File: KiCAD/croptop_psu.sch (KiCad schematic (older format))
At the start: 40 parts, among them J3 5V USB, U2 REG71055, U3 FAN5333BSX, U4 MIC23050, U5 TC1014

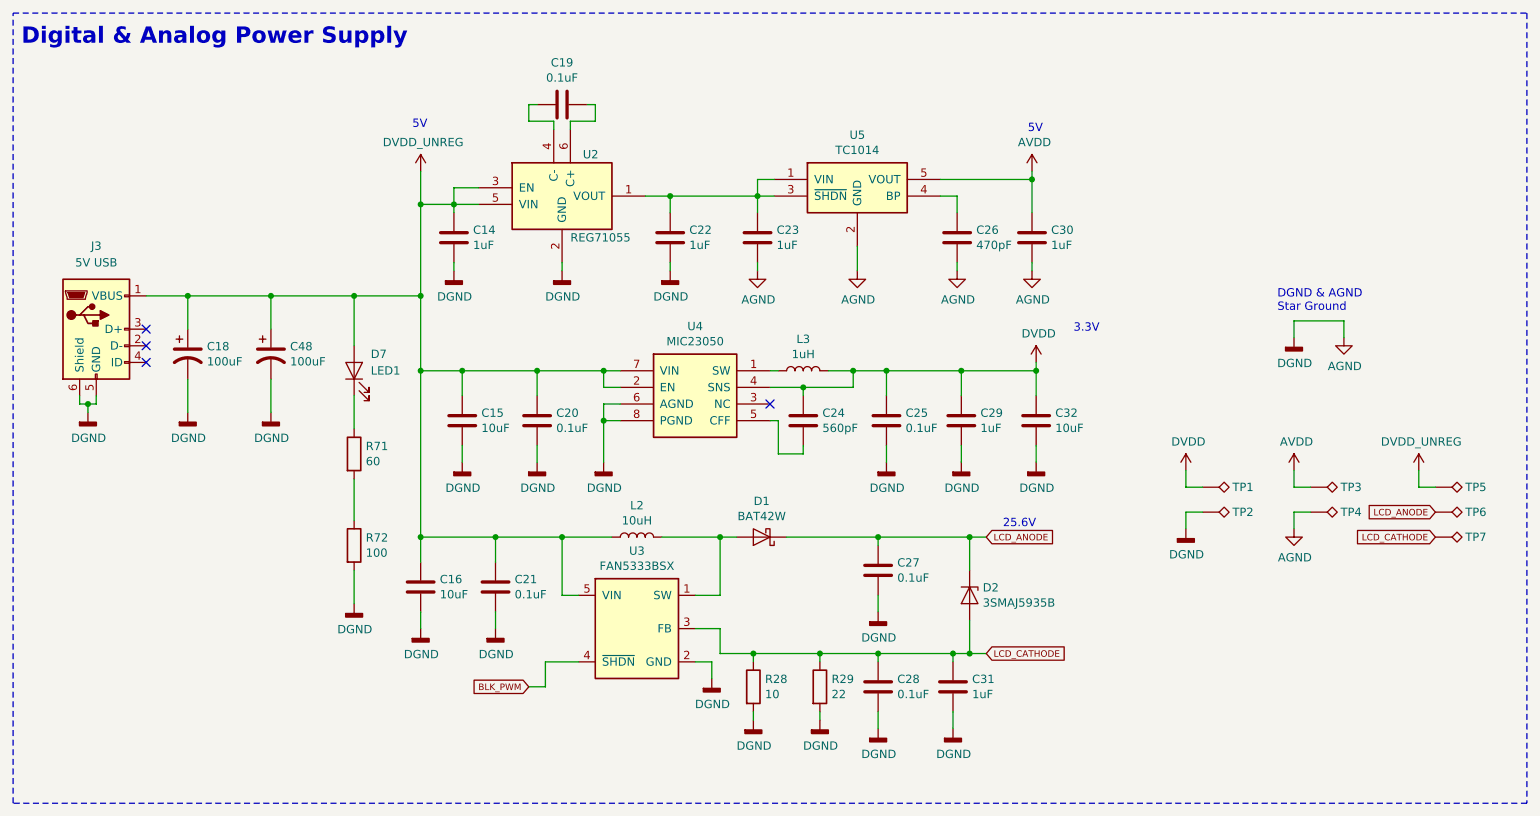
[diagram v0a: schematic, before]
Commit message: Got to PCB layout
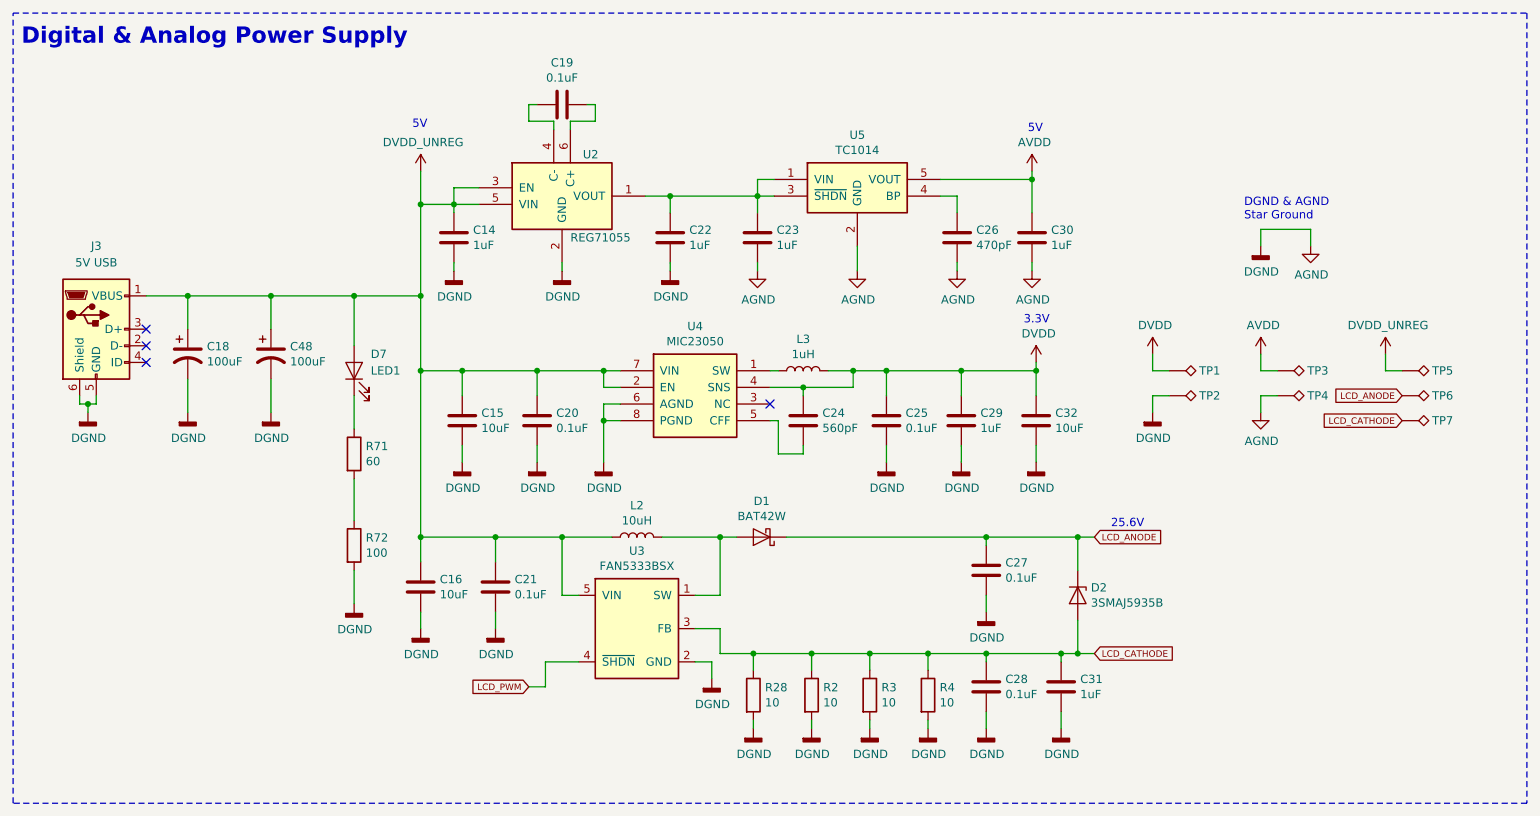
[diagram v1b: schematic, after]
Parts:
- removed R29: 22, Resistor_SMD:R_0402_1005Metric, symbol Device:R
- added R2, R3, R4: 10, Resistor_SMD:R_0402_1005Metric, symbol Device:R
- D1: footprint (none) -> croptop:D_SOD-123
- D2: footprint (none) -> croptop:DO-214AC
- J3: footprint (none) -> croptop:USB_Micro-B_Molex_47346-0001
- L2: footprint (none) -> Inductor_SMD:L_1210_3225Metric
- L3: footprint (none) -> Inductor_SMD:L_0805_2012Metric
- U4: footprint Package_DFN_QFN:Micrel_MLF-8-1EP_2x2mm_P0.5mm_EP0.8x1.3mm_ThermalVias -> Package_DFN_QFN:DFN-8-1EP_2x2mm_P0.45mm_EP0.64x1.38mm
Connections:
- net AGND: now also R2.2, R3.2, R4.2
- net LCD_CATHODE: now also R2.1, R3.1, R4.1
- net BLK_PWM renamed LCD_PWM
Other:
- moved on the sheet: C27, C28, C31, D2, R28, TP1, TP2, TP3, TP4, TP5, TP6, TP7

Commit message: Final board shape
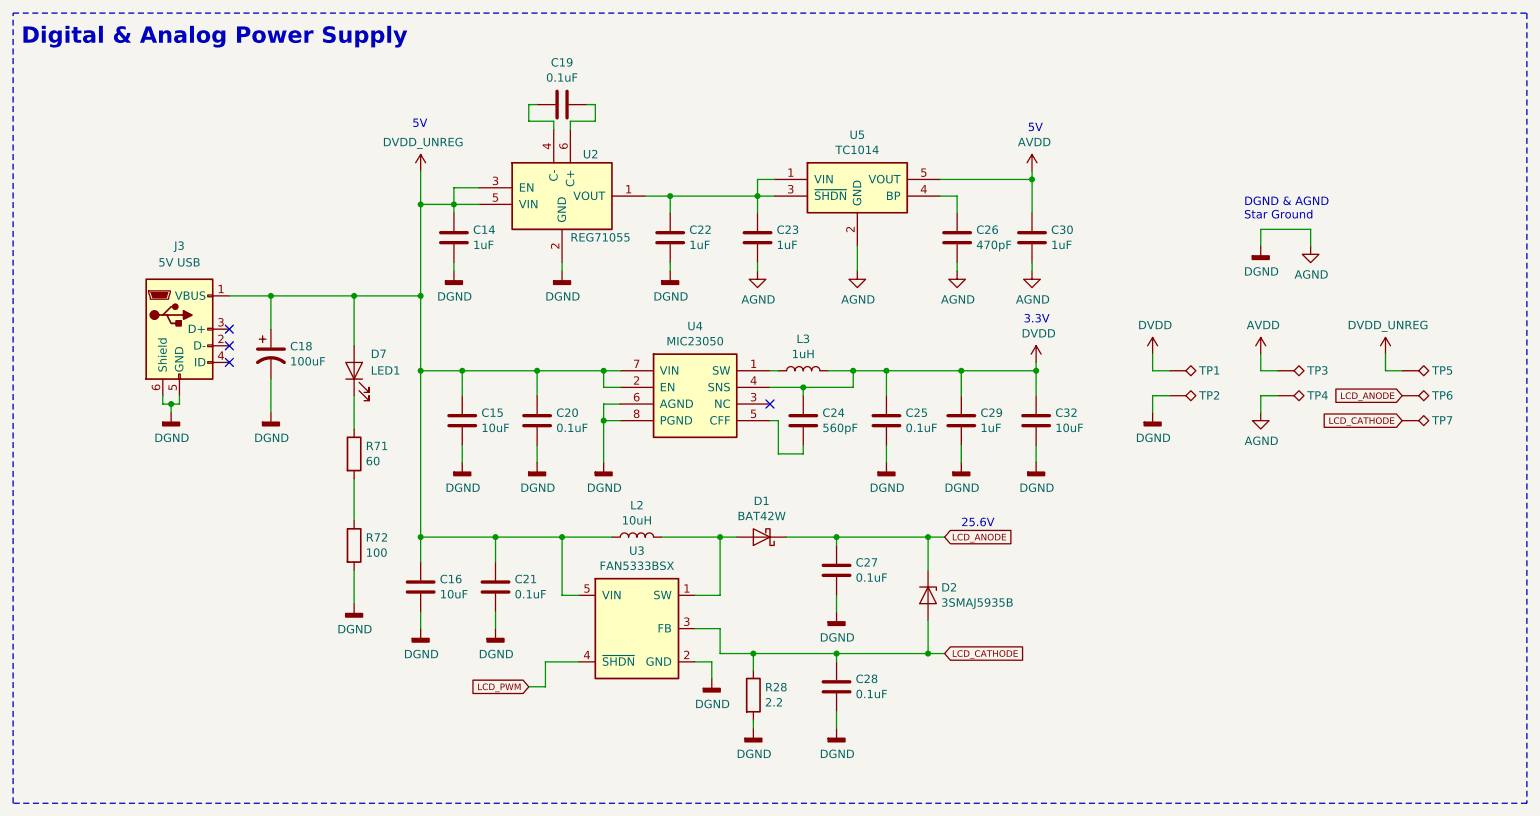
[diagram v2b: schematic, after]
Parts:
- removed C31: 1uF, Capacitor_SMD:C_0402_1005Metric, symbol Device:C
- removed C48: 100uF, Capacitor_SMD:CP_Elec_6.3x7.7, symbol Device:CP1
- removed R2, R3, R4: 10, Resistor_SMD:R_0402_1005Metric, symbol Device:R
- R28: value 10 -> 2.2
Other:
- moved on the sheet: C18, C27, C28, D2, J3

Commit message: Finished working board
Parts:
- removed C29: 1uF, Capacitor_SMD:C_0402_1005Metric, symbol Device:C
- removed TP4: TestPoint_Alt, TestPoint:TestPoint_Pad_D2.0mm, symbol Connector:TestPoint_Alt
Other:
- moved on the sheet: C32
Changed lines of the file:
@@
 Connection ~ 6000 3750
 Wire Wire Line
-	7100 4300 7100 4200
+	6800 4300 6800 4200
 $Comp
 L Device:C C32
 U 1 1 5C0134A8
-P 7100 4050
-F 0 "C32" H 7215 4096 50  0000 L CNN
-F 1 "10uF" H 7215 4005 50  0000 L CNN
-F 2 "Capacitor_SMD:C_0805_2012Metric" H 7138 3900 50  0001 C CNN
-F 3 "~" H 7100 4050 50  0001 C CNN
-	1    7100 4050
-	1    0    0    -1
-$EndComp
-Wire Wire Line
-	6650 4200 6650 4300
+P 6800 4050
+F 0 "C32" H 6915 4096 50  0000 L CNN
+F 1 "10uF" H 6915 4005 50  0000 L CNN
+F 2 "Capacitor_SMD:C_0805_2012Metric" H 6838 3900 50  0001 C CNN
+F 3 "~" H 6800 4050 50  0001 C CNN
+	1    6800 4050
+	1    0    0    -1
+$EndComp
 $Comp
 L Device:C C25
@@
 	1    0    0    -1
 $EndComp
-$Comp
-L Device:C C29
-U 1 1 5C0134BD
-P 6650 4050
-F 0 "C29" H 6765 4096 50  0000 L CNN
-F 1 "1uF" H 6765 4005 50  0000 L CNN
-F 2 "Capacitor_SMD:C_0402_1005Metric" H 6688 3900 50  0001 C CNN
-F 3 "~" H 6650 4050 50  0001 C CNN
-	1    6650 4050
-	1    0    0    -1
-$EndComp
 Wire Wire Line
 	6200 4200 6200 4300
 Wire Wire Line
-	7100 3750 7100 3900
-Wire Wire Line
-	6650 3750 6650 3900
+	6800 3750 6800 3900
 Wire Wire Line
 	6200 3750 6200 3900
 Connection ~ 6200 3750
-Connection ~ 6650 3750
 Wire Wire Line
 	6000 3750 6200 3750
 Wire Wire Line
-	6200 3750 6650 3750
-Wire Wire Line
-	6650 3750 7100 3750
-Wire Wire Line
 	7100 3700 7100 3750
-Connection ~ 7100 3750
 Wire Wire Line
 	3400 5300 3400 5200
@@
 $EndComp
 $Comp
-L CropTop:DGND #PWR044
-U 1 1 5C361545
-P 6650 4300
-F 0 "#PWR044" H 6650 4050 50  0001 C CNN
-F 1 "DGND" H 6654 4145 50  0000 C CNN
-F 2 "" H 6650 4300 50  0001 C CNN
-F 3 "" H 6650 4300 50  0001 C CNN
-	1    6650 4300
-	1    0    0    -1
-$EndComp
-$Comp
 L CropTop:DGND #PWR049
 U 1 1 5C3656D3
-P 7100 4300
-F 0 "#PWR049" H 7100 4050 50  0001 C CNN
-F 1 "DGND" H 7104 4145 50  0000 C CNN
-F 2 "" H 7100 4300 50  0001 C CNN
-F 3 "" H 7100 4300 50  0001 C CNN
-	1    7100 4300
+P 6800 4300
+F 0 "#PWR049" H 6800 4050 50  0001 C CNN
+F 1 "DGND" H 6804 4145 50  0000 C CNN
+F 2 "" H 6800 4300 50  0001 C CNN
+F 3 "" H 6800 4300 50  0001 C CNN
+	1    6800 4300
 	1    0    0    -1
 $EndComp
@@
 F 3 "" H 9200 3650 50  0001 C CNN
 	1    9200 3650
-	1    0    0    -1
-$EndComp
-$Comp
-L CropTop:AGND #PWR054
-U 1 1 5C9C4F69
-P 8450 4000
-F 0 "#PWR054" H 8450 3750 50  0001 C CNN
-F 1 "AGND" H 8455 3827 50  0000 C CNN
-F 2 "" H 8450 4000 50  0001 C CNN
-F 3 "" H 8450 4000 50  0001 C CNN
-	1    8450 4000
-	1    0    0    -1
-$EndComp
-$Comp
-L CropTop:DGND #PWR051
-U 1 1 5C9C4F6F
-P 7800 4000
-F 0 "#PWR051" H 7800 3750 50  0001 C CNN
-F 1 "DGND" H 7804 3845 50  0000 C CNN
-F 2 "" H 7800 4000 50  0001 C CNN
-F 3 "" H 7800 4000 50  0001 C CNN
-	1    7800 4000
 	1    0    0    -1
 $EndComp
@@
 $EndComp
 $Comp
-L Connector:TestPoint_Alt TP2
-U 1 1 5C9C9739
-P 7900 3900
-AR Path="/64809F0C/5C9C9739" Ref="TP2"  Part="1"
-AR Path="/66A12230/5C9C9739" Ref="TP?"  Part="1"
-AR Path="/65B709D0/5C9C9739" Ref="TP?"  Part="1"
-F 0 "TP2" V 7900 4080 50  0000 L CNN
-F 1 "TestPoint_Alt" V 7935 4085 50  0001 L CNN
-F 2 "TestPoint:TestPoint_Pad_D2.0mm" H 8100 3900 50  0001 C CNN
-F 3 "~" H 8100 3900 50  0001 C CNN
-	1    7900 3900
-	0    1    1    0
-$EndComp
-$Comp
 L Connector:TestPoint_Alt TP5
 U 1 1 5C9C9740
@@
 Wire Wire Line
 	7800 3750 7900 3750
-$Comp
-L Connector:TestPoint_Alt TP4
-U 1 1 5C9DF049
-P 8550 3900
-AR Path="/64809F0C/5C9DF049" Ref="TP4"  Part="1"
-AR Path="/66A12230/5C9DF049" Ref="TP?"  Part="1"
-AR Path="/65B709D0/5C9DF049" Ref="TP?"  Part="1"
-F 0 "TP4" V 8550 4080 50  0000 L CNN
-F 1 "TestPoint_Alt" V 8585 4085 50  0001 L CNN
-F 2 "TestPoint:TestPoint_Pad_D2.0mm" H 8750 3900 50  0001 C CNN
-F 3 "~" H 8750 3900 50  0001 C CNN
-	1    8550 3900
-	0    1    1    0
-$EndComp
-Wire Wire Line
-	8450 3900 8550 3900
-Wire Wire Line
-	8450 3900 8450 4000
-Wire Wire Line
-	7800 4000 7800 3900
-Wire Wire Line
-	7800 3900 7900 3900
 Text GLabel 9300 3900 0    39   Input ~ 0
 LCD_ANODE
@@
 Connection ~ 2500 3300
 Connection ~ 3000 3300
+Wire Wire Line
+	6200 3750 6800 3750
+Connection ~ 6800 3750
+Wire Wire Line
+	6800 3750 7100 3750
+$Comp
+L CropTop:DGND #PWR0106
+U 1 1 5C3F1F61
+P 7800 4050
+AR Path="/64809F0C/5C3F1F61" Ref="#PWR0106"  Part="1"
+AR Path="/66A12230/5C3F1F61" Ref="#PWR?"  Part="1"
+F 0 "#PWR0106" H 7800 3800 50  0001 C CNN
+F 1 "DGND" H 7804 3895 50  0000 C CNN
+F 2 "" H 7800 4050 50  0001 C CNN
+F 3 "" H 7800 4050 50  0001 C CNN
+	1    7800 4050
+	1    0    0    -1
+$EndComp
+$Comp
+L Connector:TestPoint_Alt TP2
+U 1 1 5C3F1F67
+P 7900 3950
+AR Path="/64809F0C/5C3F1F67" Ref="TP2"  Part="1"
+AR Path="/66A12230/5C3F1F67" Ref="TP?"  Part="1"
+F 0 "TP2" V 7900 4130 50  0000 L CNN
+F 1 "TestPoint_Alt" V 7935 4135 50  0001 L CNN
+F 2 "TestPoint:TestPoint_Pad_D2.0mm" H 8100 3950 50  0001 C CNN
+F 3 "~" H 8100 3950 50  0001 C CNN
+	1    7900 3950
+	0    1    1    0
+$EndComp
+Wire Wire Line
+	7800 4050 7800 3950
+Wire Wire Line
+	7800 3950 7900 3950
 $EndSCHEMATC

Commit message: Changed testpoint size
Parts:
- TP1, TP2, TP3, TP5, TP6, TP7: footprint TestPoint:TestPoint_Pad_D2.0mm -> TestPoint:TestPoint_Pad_1.0x1.0mm
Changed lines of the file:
@@
 F 0 "TP1" V 7900 3930 50  0000 L CNN
 F 1 "TestPoint_Alt" V 7935 3935 50  0001 L CNN
-F 2 "TestPoint:TestPoint_Pad_D2.0mm" H 8100 3750 50  0001 C CNN
+F 2 "TestPoint:TestPoint_Pad_1.0x1.0mm" H 8100 3750 50  0001 C CNN
 F 3 "~" H 8100 3750 50  0001 C CNN
 	1    7900 3750
@@
 F 0 "TP5" V 9300 3930 50  0000 L CNN
 F 1 "TestPoint_Alt" V 9335 3935 50  0001 L CNN
-F 2 "TestPoint:TestPoint_Pad_D2.0mm" H 9500 3750 50  0001 C CNN
+F 2 "TestPoint:TestPoint_Pad_1.0x1.0mm" H 9500 3750 50  0001 C CNN
 F 3 "~" H 9500 3750 50  0001 C CNN
 	1    9300 3750
@@
 F 0 "TP3" V 8550 3930 50  0000 L CNN
 F 1 "TestPoint_Alt" V 8585 3935 50  0001 L CNN
-F 2 "TestPoint:TestPoint_Pad_D2.0mm" H 8750 3750 50  0001 C CNN
+F 2 "TestPoint:TestPoint_Pad_1.0x1.0mm" H 8750 3750 50  0001 C CNN
 F 3 "~" H 8750 3750 50  0001 C CNN
 	1    8550 3750
@@
 F 0 "TP6" V 9300 4080 50  0000 L CNN
 F 1 "TestPoint_Alt" V 9335 4085 50  0001 L CNN
-F 2 "TestPoint:TestPoint_Pad_D2.0mm" H 9500 3900 50  0001 C CNN
+F 2 "TestPoint:TestPoint_Pad_1.0x1.0mm" H 9500 3900 50  0001 C CNN
 F 3 "~" H 9500 3900 50  0001 C CNN
 	1    9300 3900
@@
 F 0 "TP7" V 9300 4230 50  0000 L CNN
 F 1 "TestPoint_Alt" V 9335 4235 50  0001 L CNN
-F 2 "TestPoint:TestPoint_Pad_D2.0mm" H 9500 4050 50  0001 C CNN
+F 2 "TestPoint:TestPoint_Pad_1.0x1.0mm" H 9500 4050 50  0001 C CNN
 F 3 "~" H 9500 4050 50  0001 C CNN
 	1    9300 4050
@@
 F 0 "TP2" V 7900 4130 50  0000 L CNN
 F 1 "TestPoint_Alt" V 7935 4135 50  0001 L CNN
-F 2 "TestPoint:TestPoint_Pad_D2.0mm" H 8100 3950 50  0001 C CNN
+F 2 "TestPoint:TestPoint_Pad_1.0x1.0mm" H 8100 3950 50  0001 C CNN
 F 3 "~" H 8100 3950 50  0001 C CNN
 	1    7900 3950

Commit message: Complete PCB version 1
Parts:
- R28: footprint Resistor_SMD:R_0402_1005Metric -> Resistor_SMD:R_0603_1608Metric
- TP1, TP2, TP3, TP5, TP6, TP7: footprint TestPoint:TestPoint_Pad_1.0x1.0mm -> croptop:TestPoint
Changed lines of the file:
@@
 F 0 "R28" H 5470 5746 50  0000 L CNN
 F 1 "2.2" H 5470 5655 50  0000 L CNN
-F 2 "Resistor_SMD:R_0402_1005Metric" V 5330 5700 50  0001 C CNN
+F 2 "Resistor_SMD:R_0603_1608Metric" V 5330 5700 50  0001 C CNN
 F 3 "~" H 5400 5700 50  0001 C CNN
 	1    5400 5700
@@
 F 0 "TP1" V 7900 3930 50  0000 L CNN
 F 1 "TestPoint_Alt" V 7935 3935 50  0001 L CNN
-F 2 "TestPoint:TestPoint_Pad_1.0x1.0mm" H 8100 3750 50  0001 C CNN
+F 2 "croptop:TestPoint" H 8100 3750 50  0001 C CNN
 F 3 "~" H 8100 3750 50  0001 C CNN
 	1    7900 3750
@@
 F 0 "TP5" V 9300 3930 50  0000 L CNN
 F 1 "TestPoint_Alt" V 9335 3935 50  0001 L CNN
-F 2 "TestPoint:TestPoint_Pad_1.0x1.0mm" H 9500 3750 50  0001 C CNN
+F 2 "croptop:TestPoint" H 9500 3750 50  0001 C CNN
 F 3 "~" H 9500 3750 50  0001 C CNN
 	1    9300 3750
@@
 F 0 "TP3" V 8550 3930 50  0000 L CNN
 F 1 "TestPoint_Alt" V 8585 3935 50  0001 L CNN
-F 2 "TestPoint:TestPoint_Pad_1.0x1.0mm" H 8750 3750 50  0001 C CNN
+F 2 "croptop:TestPoint" H 8750 3750 50  0001 C CNN
 F 3 "~" H 8750 3750 50  0001 C CNN
 	1    8550 3750
@@
 F 0 "TP6" V 9300 4080 50  0000 L CNN
 F 1 "TestPoint_Alt" V 9335 4085 50  0001 L CNN
-F 2 "TestPoint:TestPoint_Pad_1.0x1.0mm" H 9500 3900 50  0001 C CNN
+F 2 "croptop:TestPoint" H 9500 3900 50  0001 C CNN
 F 3 "~" H 9500 3900 50  0001 C CNN
 	1    9300 3900
@@
 F 0 "TP7" V 9300 4230 50  0000 L CNN
 F 1 "TestPoint_Alt" V 9335 4235 50  0001 L CNN
-F 2 "TestPoint:TestPoint_Pad_1.0x1.0mm" H 9500 4050 50  0001 C CNN
+F 2 "croptop:TestPoint" H 9500 4050 50  0001 C CNN
 F 3 "~" H 9500 4050 50  0001 C CNN
 	1    9300 4050
@@
 F 0 "TP2" V 7900 4130 50  0000 L CNN
 F 1 "TestPoint_Alt" V 7935 4135 50  0001 L CNN
-F 2 "TestPoint:TestPoint_Pad_1.0x1.0mm" H 8100 3950 50  0001 C CNN
+F 2 "croptop:TestPoint" H 8100 3950 50  0001 C CNN
 F 3 "~" H 8100 3950 50  0001 C CNN
 	1    7900 3950
